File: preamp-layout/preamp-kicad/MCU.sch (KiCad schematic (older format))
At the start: 10 parts, among them J15 Conn_01x15_Female, J16 Conn_01x15_Female, J17 Conn_01x06_Female, J18 Conn_01x03_Female, J19 Conn_01x03_Female, J20 Conn_01x03_Female, J21 Conn_01x03_Male, J22 Conn_01x02_Female, J23 Conn_01x02_Male, U5 ESP32-DevKitC

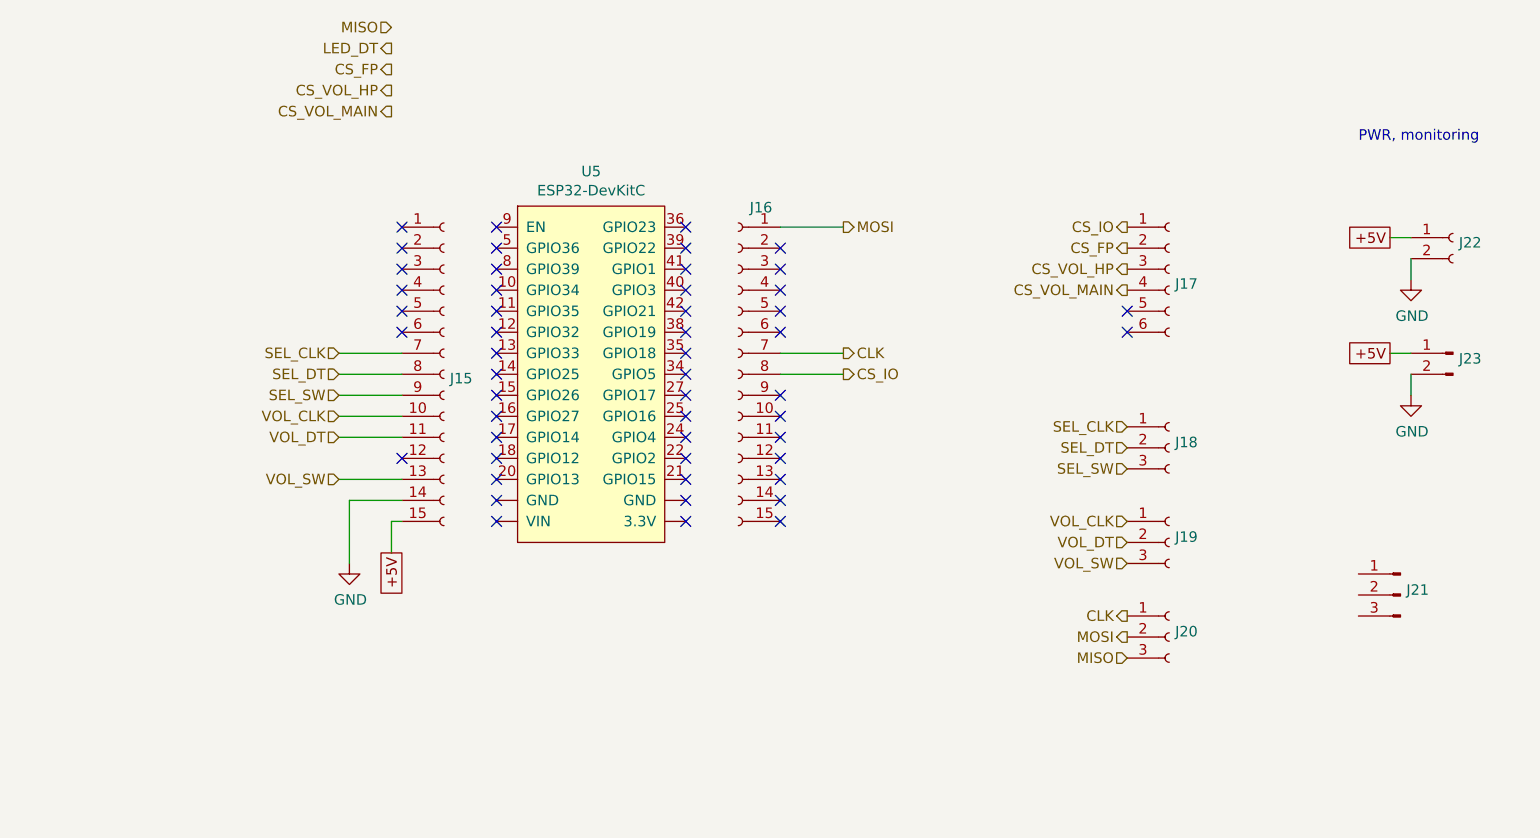
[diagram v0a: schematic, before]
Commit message: AC PCB Update
Removed Switch symbol from PCB, moved to main sheet. Started playing with footprint assignment. Other minor updates.
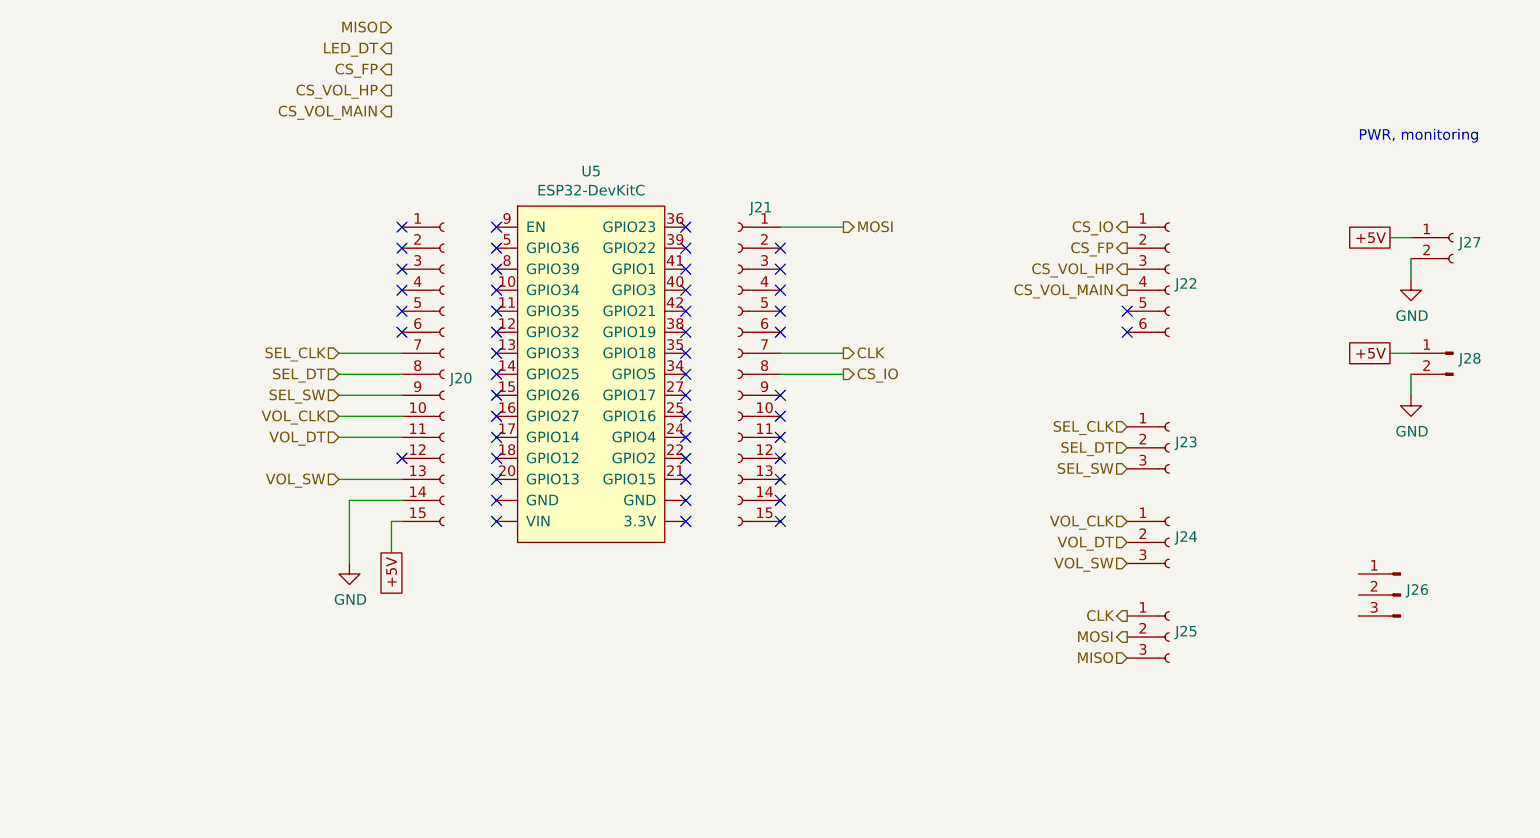
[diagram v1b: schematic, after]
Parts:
- renumbered J15 to J20, J16 to J21, J17 to J22, J18 to J23, J19 to J24, J20 to J25, J21 to J26, J22 to J27, J23 to J28
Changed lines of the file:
@@
 P 9700 2550
 AR Path="/5E2D8DA2/63AD6B3B" Ref="J?"  Part="1"
-AR Path="/619FA14B/63AD6B3B" Ref="J22"  Part="1"
-F 0 "J22" H 9728 2526 50  0000 L CNN
+AR Path="/619FA14B/63AD6B3B" Ref="J27"  Part="1"
+F 0 "J27" H 9728 2526 50  0000 L CNN
 F 1 "Conn_01x02_Female" H 9728 2435 50  0001 L CNN
 F 2 "" H 9700 2550 50  0001 C CNN
@@
 PWR, monitoring
 $Comp
-L Connector:Conn_01x02_Male J23
+L Connector:Conn_01x02_Male J28
 U 1 1 63AD6EFD
 P 9700 3100
-F 0 "J23" H 9672 3074 50  0000 R CNN
+F 0 "J28" H 9672 3074 50  0000 R CNN
 F 1 "Conn_01x02_Male" H 9672 2983 50  0001 R CNN
 F 2 "" H 9700 3100 50  0001 C CNN
@@
 AR Path="/5E607732/6496C10E" Ref="J?"  Part="1"
 AR Path="/5E2D8DA2/6496C10E" Ref="J?"  Part="1"
-AR Path="/619FA14B/6496C10E" Ref="J18"  Part="1"
-F 0 "J18" H 8378 3576 50  0000 L CNN
+AR Path="/619FA14B/6496C10E" Ref="J23"  Part="1"
+F 0 "J23" H 8378 3576 50  0000 L CNN
 F 1 "Conn_01x03_Female" H 8378 3485 50  0001 L CNN
 F 2 "" H 8350 3550 50  0001 C CNN
@@
 P 9450 4250
 AR Path="/5E2D8DA2/6496C114" Ref="J?"  Part="1"
-AR Path="/619FA14B/6496C114" Ref="J21"  Part="1"
-F 0 "J21" H 9422 4274 50  0000 R CNN
+AR Path="/619FA14B/6496C114" Ref="J26"  Part="1"
+F 0 "J26" H 9422 4274 50  0000 R CNN
 F 1 "Conn_01x03_Male" H 9422 4183 50  0001 R CNN
 F 2 "" H 9450 4250 50  0001 C CNN
@@
 AR Path="/5E607732/6496FD14" Ref="J?"  Part="1"
 AR Path="/5E2D8DA2/6496FD14" Ref="J?"  Part="1"
-AR Path="/619FA14B/6496FD14" Ref="J19"  Part="1"
-F 0 "J19" H 8378 4026 50  0000 L CNN
+AR Path="/619FA14B/6496FD14" Ref="J24"  Part="1"
+F 0 "J24" H 8378 4026 50  0000 L CNN
 F 1 "Conn_01x03_Female" H 8378 3935 50  0001 L CNN
 F 2 "" H 8350 4000 50  0001 C CNN
@@
 AR Path="/5E607732/64973E6E" Ref="J?"  Part="1"
 AR Path="/5E2D8DA2/64973E6E" Ref="J?"  Part="1"
-AR Path="/619FA14B/64973E6E" Ref="J20"  Part="1"
-F 0 "J20" H 8378 4476 50  0000 L CNN
+AR Path="/619FA14B/64973E6E" Ref="J25"  Part="1"
+F 0 "J25" H 8378 4476 50  0000 L CNN
 F 1 "Conn_01x03_Female" H 8378 4385 50  0001 L CNN
 F 2 "" H 8350 4450 50  0001 C CNN
@@
 MISO
 $Comp
-L Connector:Conn_01x06_Female J17
+L Connector:Conn_01x06_Female J22
 U 1 1 64977856
 P 8350 2700
-F 0 "J17" H 8378 2630 50  0000 L CNN
+F 0 "J22" H 8378 2630 50  0000 L CNN
 F 1 "Conn_01x06_Female" H 8378 2585 50  0001 L CNN
 F 2 "" H 8350 2700 50  0001 C CNN
@@
 CS_IO
 $Comp
-L Connector:Conn_01x15_Female J16
+L Connector:Conn_01x15_Female J21
 U 1 1 649C22F5
 P 6300 3200
-F 0 "J16" H 6192 3993 50  0000 C CNN
+F 0 "J21" H 6192 3993 50  0000 C CNN
 F 1 "Conn_01x15_Female" H 6192 3994 50  0001 C CNN
 F 2 "" H 6300 3200 50  0001 C CNN
@@
 $EndComp
 $Comp
-L Connector:Conn_01x15_Female J15
+L Connector:Conn_01x15_Female J20
 U 1 1 649C438C
 P 4900 3200
-F 0 "J15" H 4928 3180 50  0000 L CNN
+F 0 "J20" H 4928 3180 50  0000 L CNN
 F 1 "Conn_01x15_Female" H 4928 3135 50  0001 L CNN
 F 2 "" H 4900 3200 50  0001 C CNN

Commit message: Initial Footprint Assignment
Assigned footprints to SMT resistors, pin headers, screw terminals, LEDs, DIP-8 ICs
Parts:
- J20, J21: footprint (none) -> Connector_PinHeader_2.54mm:PinHeader_1x15_P2.54mm_Vertical
- J22: footprint (none) -> Connector_PinHeader_2.54mm:PinHeader_1x06_P2.54mm_Vertical
- J23, J24, J25, J26: footprint (none) -> Connector_PinHeader_2.54mm:PinHeader_1x03_P2.54mm_Vertical
- J27, J28: footprint (none) -> Connector_PinHeader_2.54mm:PinHeader_1x02_P2.54mm_Vertical
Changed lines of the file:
@@
 F 0 "J27" H 9728 2526 50  0000 L CNN
 F 1 "Conn_01x02_Female" H 9728 2435 50  0001 L CNN
-F 2 "" H 9700 2550 50  0001 C CNN
+F 2 "Connector_PinHeader_2.54mm:PinHeader_1x02_P2.54mm_Vertical" H 9700 2550 50  0001 C CNN
 F 3 "~" H 9700 2550 50  0001 C CNN
 	1    9700 2550
@@
 F 0 "J28" H 9672 3074 50  0000 R CNN
 F 1 "Conn_01x02_Male" H 9672 2983 50  0001 R CNN
-F 2 "" H 9700 3100 50  0001 C CNN
+F 2 "Connector_PinHeader_2.54mm:PinHeader_1x02_P2.54mm_Vertical" H 9700 3100 50  0001 C CNN
 F 3 "~" H 9700 3100 50  0001 C CNN
 	1    9700 3100
@@
 F 0 "J23" H 8378 3576 50  0000 L CNN
 F 1 "Conn_01x03_Female" H 8378 3485 50  0001 L CNN
-F 2 "" H 8350 3550 50  0001 C CNN
+F 2 "Connector_PinHeader_2.54mm:PinHeader_1x03_P2.54mm_Vertical" H 8350 3550 50  0001 C CNN
 F 3 "~" H 8350 3550 50  0001 C CNN
 	1    8350 3550
@@
 F 0 "J26" H 9422 4274 50  0000 R CNN
 F 1 "Conn_01x03_Male" H 9422 4183 50  0001 R CNN
-F 2 "" H 9450 4250 50  0001 C CNN
+F 2 "Connector_PinHeader_2.54mm:PinHeader_1x03_P2.54mm_Vertical" H 9450 4250 50  0001 C CNN
 F 3 "~" H 9450 4250 50  0001 C CNN
 	1    9450 4250
@@
 F 0 "J24" H 8378 4026 50  0000 L CNN
 F 1 "Conn_01x03_Female" H 8378 3935 50  0001 L CNN
-F 2 "" H 8350 4000 50  0001 C CNN
+F 2 "Connector_PinHeader_2.54mm:PinHeader_1x03_P2.54mm_Vertical" H 8350 4000 50  0001 C CNN
 F 3 "~" H 8350 4000 50  0001 C CNN
 	1    8350 4000
@@
 F 0 "J25" H 8378 4476 50  0000 L CNN
 F 1 "Conn_01x03_Female" H 8378 4385 50  0001 L CNN
-F 2 "" H 8350 4450 50  0001 C CNN
+F 2 "Connector_PinHeader_2.54mm:PinHeader_1x03_P2.54mm_Vertical" H 8350 4450 50  0001 C CNN
 F 3 "~" H 8350 4450 50  0001 C CNN
 	1    8350 4450
@@
 F 0 "J22" H 8378 2630 50  0000 L CNN
 F 1 "Conn_01x06_Female" H 8378 2585 50  0001 L CNN
-F 2 "" H 8350 2700 50  0001 C CNN
+F 2 "Connector_PinHeader_2.54mm:PinHeader_1x06_P2.54mm_Vertical" H 8350 2700 50  0001 C CNN
 F 3 "~" H 8350 2700 50  0001 C CNN
 	1    8350 2700
@@
 F 0 "J21" H 6192 3993 50  0000 C CNN
 F 1 "Conn_01x15_Female" H 6192 3994 50  0001 C CNN
-F 2 "" H 6300 3200 50  0001 C CNN
+F 2 "Connector_PinHeader_2.54mm:PinHeader_1x15_P2.54mm_Vertical" H 6300 3200 50  0001 C CNN
 F 3 "~" H 6300 3200 50  0001 C CNN
 	1    6300 3200
@@
 F 0 "J20" H 4928 3180 50  0000 L CNN
 F 1 "Conn_01x15_Female" H 4928 3135 50  0001 L CNN
-F 2 "" H 4900 3200 50  0001 C CNN
+F 2 "Connector_PinHeader_2.54mm:PinHeader_1x15_P2.54mm_Vertical" H 4900 3200 50  0001 C CNN
 F 3 "~" H 4900 3200 50  0001 C CNN
 	1    4900 3200

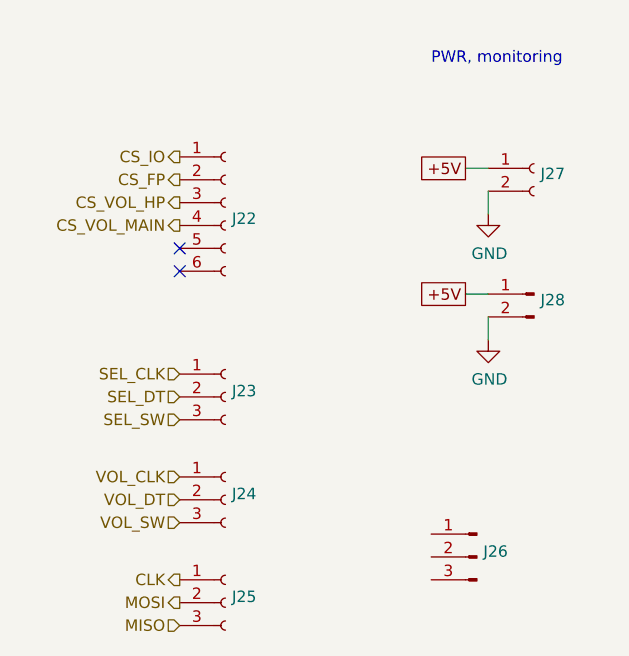
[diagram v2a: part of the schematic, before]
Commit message: BOM update
Minor changes to schematic, value changes and footprint entry. BOM updated with parts sourcing
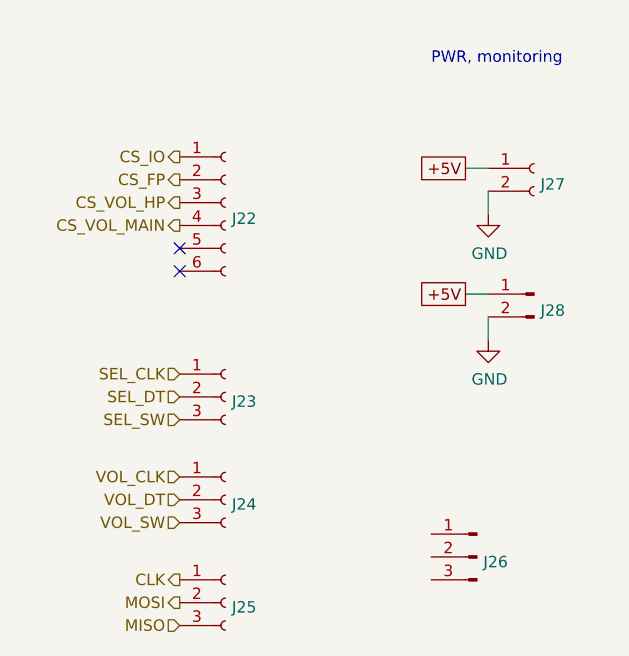
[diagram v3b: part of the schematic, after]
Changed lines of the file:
@@
 AR Path="/5E2D8DA2/63AD6B3B" Ref="J?"  Part="1"
 AR Path="/619FA14B/63AD6B3B" Ref="J27"  Part="1"
-F 0 "J27" H 9728 2526 50  0000 L CNN
+F 0 "J27" H 9728 2480 50  0000 L CNN
 F 1 "Conn_01x02_Female" H 9728 2435 50  0001 L CNN
 F 2 "Connector_PinHeader_2.54mm:PinHeader_1x02_P2.54mm_Vertical" H 9700 2550 50  0001 C CNN
@@
 U 1 1 63AD6EFD
 P 9700 3100
-F 0 "J28" H 9672 3074 50  0000 R CNN
+F 0 "J28" H 9672 3028 50  0000 R CNN
 F 1 "Conn_01x02_Male" H 9672 2983 50  0001 R CNN
 F 2 "Connector_PinHeader_2.54mm:PinHeader_1x02_P2.54mm_Vertical" H 9700 3100 50  0001 C CNN
@@
 AR Path="/5E2D8DA2/6496C10E" Ref="J?"  Part="1"
 AR Path="/619FA14B/6496C10E" Ref="J23"  Part="1"
-F 0 "J23" H 8378 3576 50  0000 L CNN
+F 0 "J23" H 8378 3530 50  0000 L CNN
 F 1 "Conn_01x03_Female" H 8378 3485 50  0001 L CNN
 F 2 "Connector_PinHeader_2.54mm:PinHeader_1x03_P2.54mm_Vertical" H 8350 3550 50  0001 C CNN
@@
 AR Path="/5E2D8DA2/6496C114" Ref="J?"  Part="1"
 AR Path="/619FA14B/6496C114" Ref="J26"  Part="1"
-F 0 "J26" H 9422 4274 50  0000 R CNN
+F 0 "J26" H 9422 4228 50  0000 R CNN
 F 1 "Conn_01x03_Male" H 9422 4183 50  0001 R CNN
 F 2 "Connector_PinHeader_2.54mm:PinHeader_1x03_P2.54mm_Vertical" H 9450 4250 50  0001 C CNN
@@
 AR Path="/5E2D8DA2/6496FD14" Ref="J?"  Part="1"
 AR Path="/619FA14B/6496FD14" Ref="J24"  Part="1"
-F 0 "J24" H 8378 4026 50  0000 L CNN
+F 0 "J24" H 8378 3980 50  0000 L CNN
 F 1 "Conn_01x03_Female" H 8378 3935 50  0001 L CNN
 F 2 "Connector_PinHeader_2.54mm:PinHeader_1x03_P2.54mm_Vertical" H 8350 4000 50  0001 C CNN
@@
 AR Path="/5E2D8DA2/64973E6E" Ref="J?"  Part="1"
 AR Path="/619FA14B/64973E6E" Ref="J25"  Part="1"
-F 0 "J25" H 8378 4476 50  0000 L CNN
+F 0 "J25" H 8378 4430 50  0000 L CNN
 F 1 "Conn_01x03_Female" H 8378 4385 50  0001 L CNN
 F 2 "Connector_PinHeader_2.54mm:PinHeader_1x03_P2.54mm_Vertical" H 8350 4450 50  0001 C CNN

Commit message: power headers updated, slight BOM update
changed footprint on all 5V, +-15V to JST B2B / B3B connectors. All male conns now.
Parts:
- removed J27: Conn_01x02_Female, Connector_PinHeader_2.54mm:PinHeader_1x02_P2.54mm_Vertical, symbol Connector:Conn_01x02_Female
- added J27: Conn_01x02_Male, Connector_JST:JST_EH_B2B-EH-A_1x02_P2.50mm_Vertical, symbol Connector:Conn_01x02_Male
- J28: footprint Connector_PinHeader_2.54mm:PinHeader_1x02_P2.54mm_Vertical -> Connector_JST:JST_EH_B2B-EH-A_1x02_P2.50mm_Vertical
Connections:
- net +5V: now also J27.1 (Pin_1)
- net GND: now also J27.2 (Pin_2)
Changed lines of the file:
@@
 Text GLabel 9400 2550 0    50   UnSpc ~ 0
 +5V
-$Comp
-L Connector:Conn_01x02_Female J?
-U 1 1 63AD6B3B
-P 9700 2550
-AR Path="/5E2D8DA2/63AD6B3B" Ref="J?"  Part="1"
-AR Path="/619FA14B/63AD6B3B" Ref="J27"  Part="1"
-F 0 "J27" H 9728 2480 50  0000 L CNN
-F 1 "Conn_01x02_Female" H 9728 2435 50  0001 L CNN
-F 2 "Connector_PinHeader_2.54mm:PinHeader_1x02_P2.54mm_Vertical" H 9700 2550 50  0001 C CNN
-F 3 "~" H 9700 2550 50  0001 C CNN
-	1    9700 2550
-	1    0    0    -1
-$EndComp
 Text Notes 9250 2100 0    50   ~ 0
 PWR, monitoring
@@
 F 0 "J28" H 9672 3028 50  0000 R CNN
 F 1 "Conn_01x02_Male" H 9672 2983 50  0001 R CNN
-F 2 "Connector_PinHeader_2.54mm:PinHeader_1x02_P2.54mm_Vertical" H 9700 3100 50  0001 C CNN
+F 2 "Connector_JST:JST_EH_B2B-EH-A_1x02_P2.50mm_Vertical" H 9700 3100 50  0001 C CNN
 F 3 "~" H 9700 3100 50  0001 C CNN
 	1    9700 3100
@@
 NoConn ~ 8150 2900
 NoConn ~ 8150 3000
+$Comp
+L Connector:Conn_01x02_Male J27
+U 1 1 5E6537E3
+P 9700 2550
+F 0 "J27" H 9672 2478 50  0000 R CNN
+F 1 "Conn_01x02_Male" H 9672 2433 50  0001 R CNN
+F 2 "Connector_JST:JST_EH_B2B-EH-A_1x02_P2.50mm_Vertical" H 9700 2550 50  0001 C CNN
+F 3 "~" H 9700 2550 50  0001 C CNN
+	1    9700 2550
+	-1   0    0    -1
+$EndComp
 $EndSCHEMATC

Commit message: Transformer specification
updated schematic, BOM with power transformer info. Other minor schematic tweaks.
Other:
- moved on the sheet: J20, J21, J22, J23, J24, J25, J26, J27, J28, U5

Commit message: Added front panel LED sheet. BOM update. Front panel PCA work
other minor changes like LED color assignments, etc
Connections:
- net +5V: now also J26.1 (Pin_1)
- net GND: now also J26.3 (Pin_3)
- net LED_DT: now also J26.2 (Pin_2)
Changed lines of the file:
@@
 $Descr A4 11693 8268
 encoding utf-8
-Sheet 7 11
+Sheet 7 12
 Title "Preamp MCU Board"
 Date "2020-01-23"
@@
 Text HLabel 3550 2500 0    50   Output ~ 0
 CS_VOL_HP
-Text HLabel 3550 2300 0    50   Output ~ 0
+Text HLabel 8050 4900 0    50   Output ~ 0
 LED_DT
 Text HLabel 3550 2600 0    50   Output ~ 0
@@
 	-1   0    0    -1
 $EndComp
+Wire Wire Line
+	8050 5000 8050 5100
+$Comp
+L power:GND #PWR?
+U 1 1 5EA8A311
+P 8050 5100
+AR Path="/5E26F6FE/5EA8A311" Ref="#PWR?"  Part="1"
+AR Path="/619FA14B/5EA8A311" Ref="#PWR021"  Part="1"
+F 0 "#PWR021" H 8050 4850 50  0001 C CNN
+F 1 "GND" H 8055 4927 50  0000 C CNN
+F 2 "" H 8050 5100 50  0001 C CNN
+F 3 "" H 8050 5100 50  0001 C CNN
+	1    8050 5100
+	1    0    0    -1
+$EndComp
+Text GLabel 8050 4800 0    50   UnSpc ~ 0
++5V
+Wire Wire Line
+	8050 4800 8150 4800
+Wire Wire Line
+	8050 4900 8150 4900
+Wire Wire Line
+	8050 5000 8150 5000
 $EndSCHEMATC
